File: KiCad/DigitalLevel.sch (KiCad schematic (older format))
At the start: 67 parts, among them SW1 SW_Push_Open, SW2 SW_Push_Open, SW3 SW_Push_Open, U2 MPU-6050, U3 XC6206P332MR

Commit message: Fixed schematics
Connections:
- net DIODE-SW renamed LED-SW
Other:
- moved on the sheet: C3
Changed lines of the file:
@@
 	1250 7400 1250 7600
-Wire Wire Line
-	1250 7600 1150 7600
 Wire Wire Line
 	3050 6850 3350 6850
@@
 	3350 7400 3350 7600
 Wire Wire Line
-	3350 7600 2350 7600
-Connection ~ 1250 7600
-Wire Wire Line
 	1650 6750 1550 6750
 Wire Wire Line
@@
 Wire Wire Line
 	1550 7400 1550 7600
-Connection ~ 1550 7600
-Wire Wire Line
-	1550 7600 1250 7600
 $Comp
 L Device:C C1
@@
 Wire Wire Line
 	3800 6750 3800 7100
-Connection ~ 3350 7600
 Wire Wire Line
 	2450 5850 2450 5750
@@
 	3800 7400 3800 7600
 Wire Wire Line
-	3350 7600 3800 7600
-Wire Wire Line
 	2250 5850 2250 5750
 Wire Wire Line
-	1150 6850 1150 7600
-Wire Wire Line
-	1150 6850 1650 6850
-Connection ~ 1150 7600
-Wire Wire Line
-	1150 7600 950  7600
-Wire Wire Line
-	1150 6850 800  6850
-Wire Wire Line
-	800  6850 800  6950
-Connection ~ 1150 6850
+	800  6850 800  7600
 $Comp
 L Device:C C3
 U 1 1 5E31CE3D
-P 800 7100
-F 0 "C3" H 915 7146 50  0000 L CNN
-F 1 "0.01u" H 915 7055 50  0000 L CNN
-F 2 "" H 838 6950 50  0001 C CNN
-F 3 "~" H 800 7100 50  0001 C CNN
-	1    800  7100
-	1    0    0    -1
-$EndComp
-Wire Wire Line
-	800  7250 800  7300
-Text GLabel 800  7300 3    50   Input ~ 0
+P 800 6700
+F 0 "C3" H 915 6746 50  0000 L CNN
+F 1 "0.01u" H 915 6655 50  0000 L CNN
+F 2 "" H 838 6550 50  0001 C CNN
+F 3 "~" H 800 6700 50  0001 C CNN
+	1    800  6700
+	-1   0    0    1
+$EndComp
+Wire Wire Line
+	800  6550 800  6500
+Text GLabel 800  6500 1    50   Input ~ 0
 VCC
 Wire Wire Line
@@
 $EndComp
 Wire Wire Line
-	1800 5350 1800 5300
-Wire Wire Line
 	2250 5750 2450 5750
 Connection ~ 2450 5750
@@
 Wire Wire Line
 	2350 7250 2350 7600
-Connection ~ 2350 7600
-Wire Wire Line
-	2350 7600 1550 7600
 Text GLabel 7550 2700 0    50   Input ~ 0
 VIN
@@
 	1050 1050 1050 1000
 Text GLabel 1050 1000 1    50   Input ~ 0
-DIODE-SW
+LED-SW
 Wire Wire Line
 	10300 1700 10300 1850
@@
 L power:GND #PWR?
 U 1 1 5E6CB783
-P 950 7600
-F 0 "#PWR?" H 950 7350 50  0001 C CNN
-F 1 "GND" H 955 7427 50  0000 C CNN
-F 2 "" H 950 7600 50  0001 C CNN
-F 3 "" H 950 7600 50  0001 C CNN
-	1    950  7600
-	1    0    0    -1
-$EndComp
-Wire Wire Line
-	1800 5300 1300 5300
-Wire Wire Line
-	1800 5750 2050 5750
-Wire Wire Line
-	1800 5750 1300 5750
-Wire Wire Line
-	1300 5750 1300 5850
-Connection ~ 1800 5750
-Wire Wire Line
-	1300 5300 1300 5200
+P 800 7600
+F 0 "#PWR?" H 800 7350 50  0001 C CNN
+F 1 "GND" H 805 7427 50  0000 C CNN
+F 2 "" H 800 7600 50  0001 C CNN
+F 3 "" H 800 7600 50  0001 C CNN
+	1    800  7600
+	1    0    0    -1
+$EndComp
 $Comp
 L power:GND #PWR?
 U 1 1 5E70F339
-P 1300 5850
-F 0 "#PWR?" H 1300 5600 50  0001 C CNN
-F 1 "GND" H 1305 5677 50  0000 C CNN
-F 2 "" H 1300 5850 50  0001 C CNN
-F 3 "" H 1300 5850 50  0001 C CNN
-	1    1300 5850
+P 1800 5750
+F 0 "#PWR?" H 1800 5500 50  0001 C CNN
+F 1 "GND" H 1805 5577 50  0000 C CNN
+F 2 "" H 1800 5750 50  0001 C CNN
+F 3 "" H 1800 5750 50  0001 C CNN
+	1    1800 5750
 	1    0    0    -1
 $EndComp
@@
 	9700 5400 9700 5550
 Connection ~ 9700 5550
-Text GLabel 1300 5200 1    50   Input ~ 0
+Text GLabel 1800 5350 1    50   Input ~ 0
 VCC
 Wire Wire Line
@@
 	1050 1850 2250 1850
 Connection ~ 2250 1850
+Connection ~ 800  6850
+Wire Wire Line
+	800  6850 1650 6850
+$Comp
+L power:GND #PWR?
+U 1 1 5E9579DB
+P 1250 7600
+F 0 "#PWR?" H 1250 7350 50  0001 C CNN
+F 1 "GND" H 1255 7427 50  0000 C CNN
+F 2 "" H 1250 7600 50  0001 C CNN
+F 3 "" H 1250 7600 50  0001 C CNN
+	1    1250 7600
+	1    0    0    -1
+$EndComp
+$Comp
+L power:GND #PWR?
+U 1 1 5E95E47C
+P 1550 7600
+F 0 "#PWR?" H 1550 7350 50  0001 C CNN
+F 1 "GND" H 1555 7427 50  0000 C CNN
+F 2 "" H 1550 7600 50  0001 C CNN
+F 3 "" H 1550 7600 50  0001 C CNN
+	1    1550 7600
+	1    0    0    -1
+$EndComp
+$Comp
+L power:GND #PWR?
+U 1 1 5E964EA6
+P 2350 7600
+F 0 "#PWR?" H 2350 7350 50  0001 C CNN
+F 1 "GND" H 2355 7427 50  0000 C CNN
+F 2 "" H 2350 7600 50  0001 C CNN
+F 3 "" H 2350 7600 50  0001 C CNN
+	1    2350 7600
+	1    0    0    -1
+$EndComp
+$Comp
+L power:GND #PWR?
+U 1 1 5E96B8D8
+P 3350 7600
+F 0 "#PWR?" H 3350 7350 50  0001 C CNN
+F 1 "GND" H 3355 7427 50  0000 C CNN
+F 2 "" H 3350 7600 50  0001 C CNN
+F 3 "" H 3350 7600 50  0001 C CNN
+	1    3350 7600
+	1    0    0    -1
+$EndComp
+$Comp
+L power:GND #PWR?
+U 1 1 5E972312
+P 3800 7600
+F 0 "#PWR?" H 3800 7350 50  0001 C CNN
+F 1 "GND" H 3805 7427 50  0000 C CNN
+F 2 "" H 3800 7600 50  0001 C CNN
+F 3 "" H 3800 7600 50  0001 C CNN
+	1    3800 7600
+	1    0    0    -1
+$EndComp
 $EndSCHEMATC

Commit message: Fixed schematics
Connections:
- net VCC: now also U?.24 (VDD)
- net VOUT: now also U?.9 (VDDA)
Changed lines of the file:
@@
 	1    0    0    -1
 $EndComp
+Wire Wire Line
+	3850 2450 3850 2250
+Text GLabel 3850 2250 1    50   Output ~ 0
+VCC
+Wire Wire Line
+	4150 2450 4150 2250
+Text GLabel 4150 2250 1    50   Input ~ 0
+VOUT
 $EndSCHEMATC

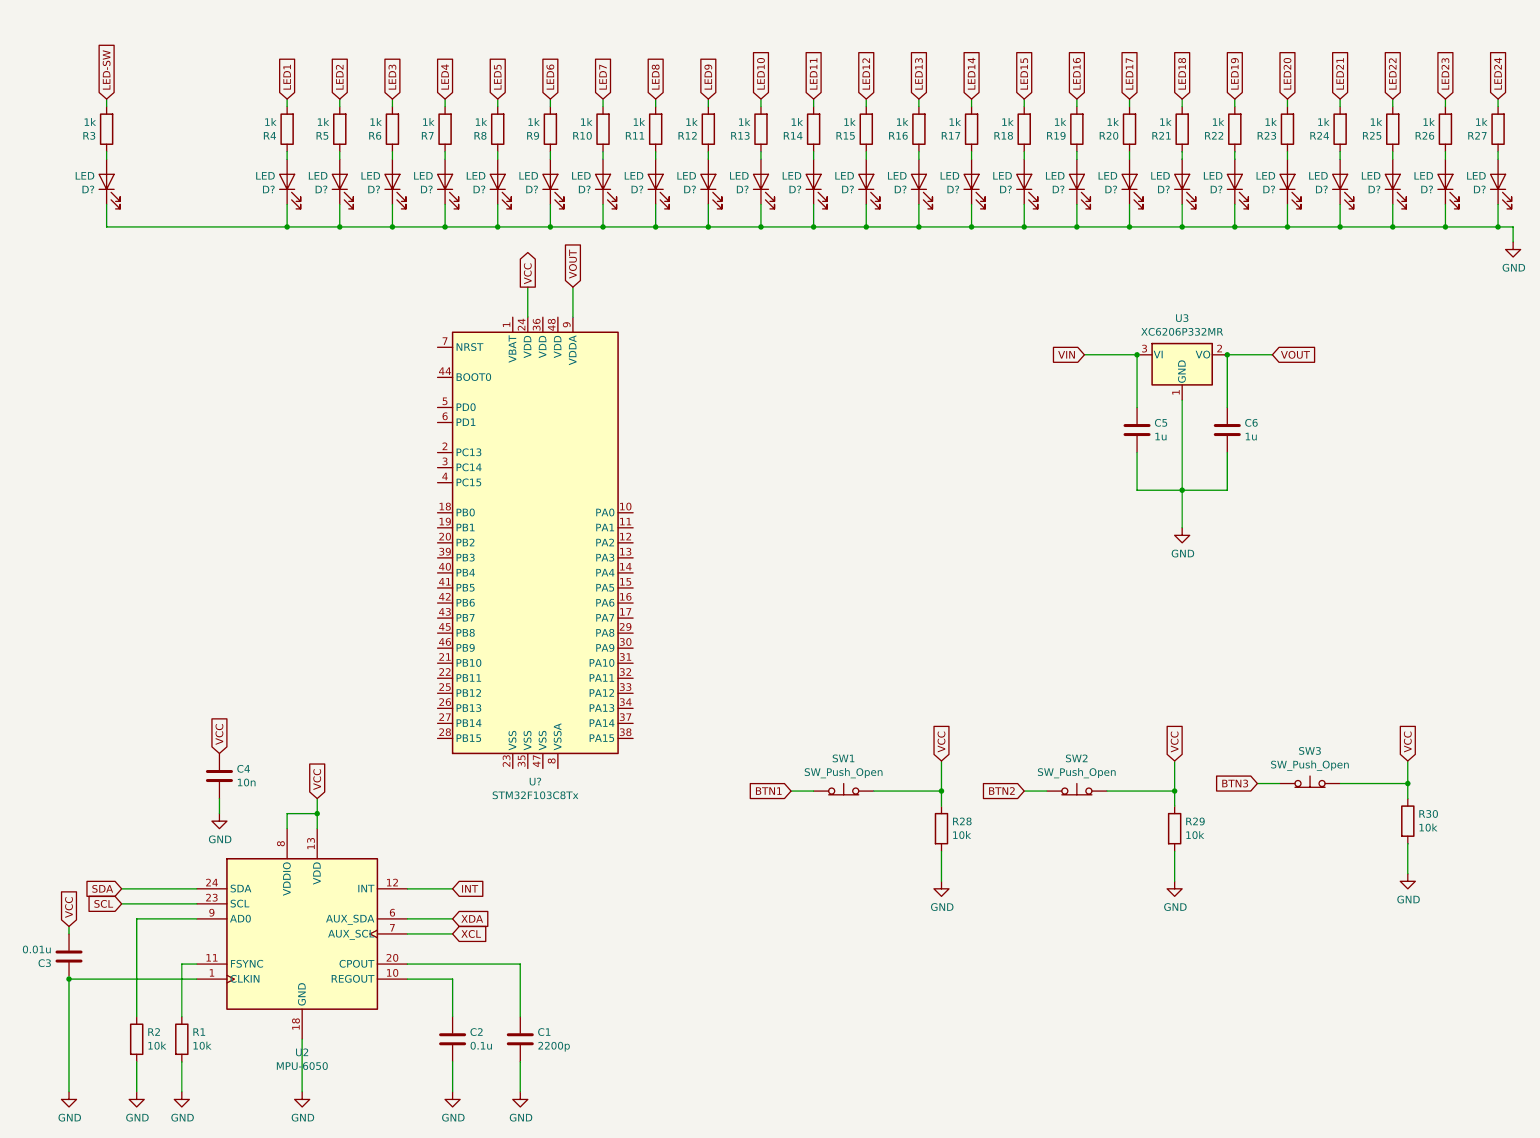
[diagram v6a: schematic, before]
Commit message: Fixed schematics
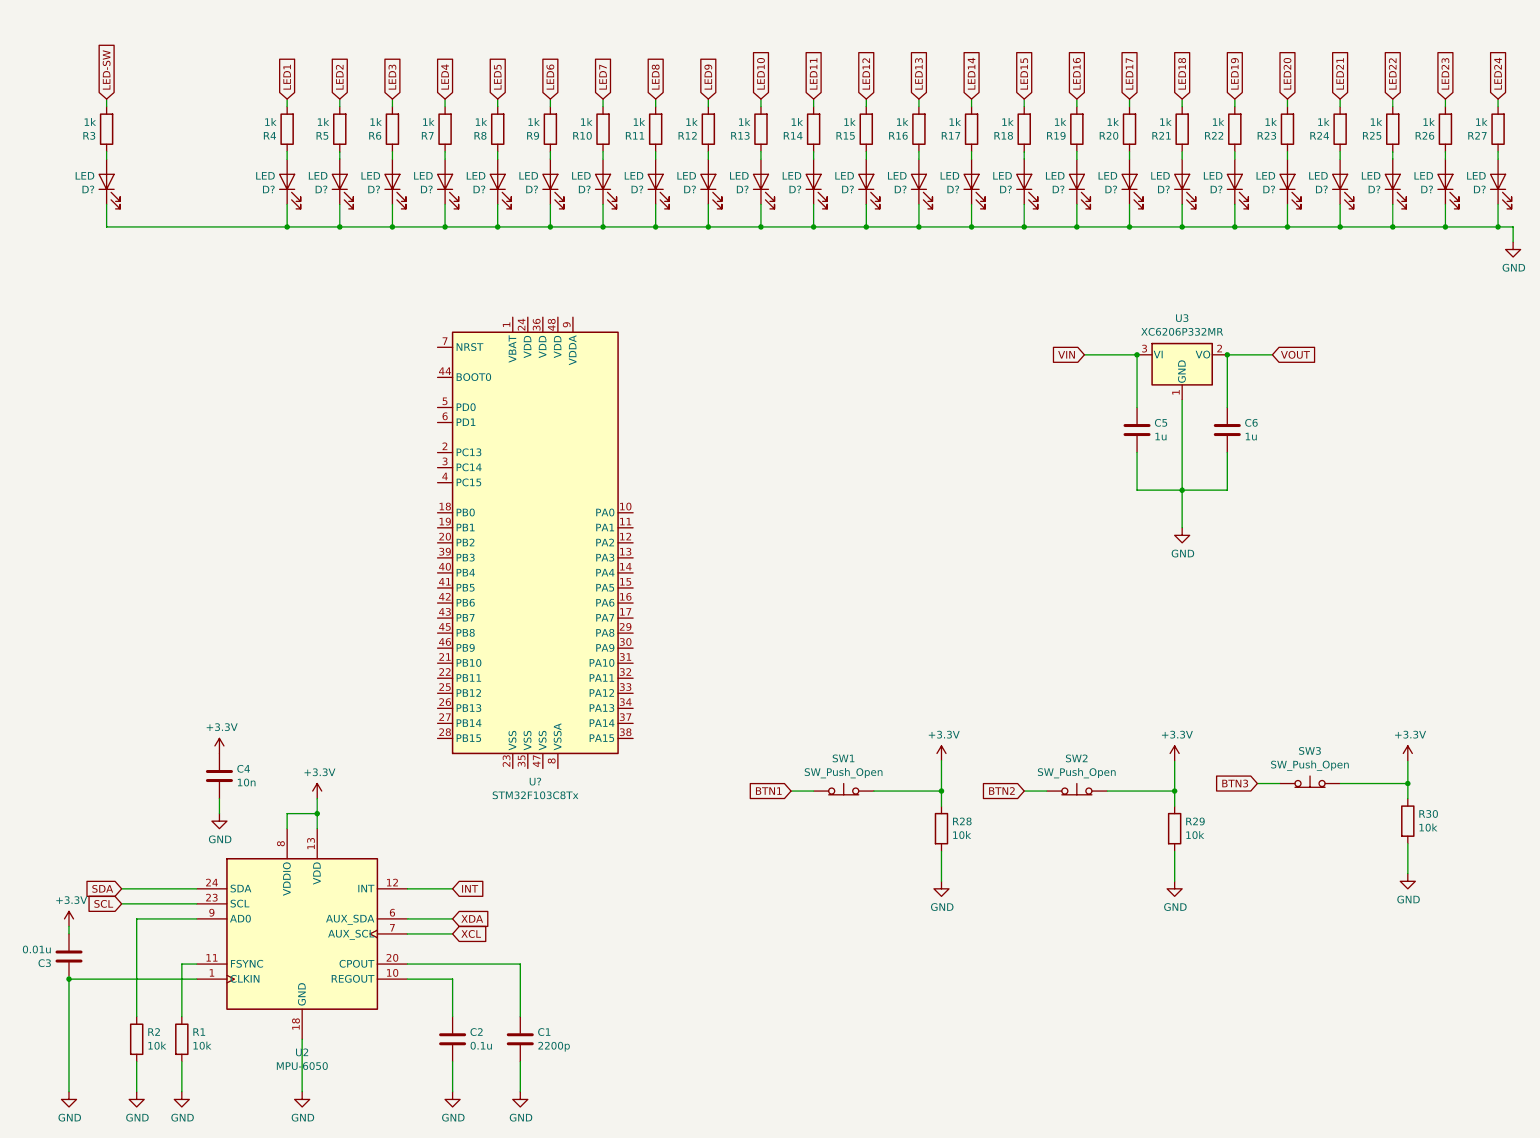
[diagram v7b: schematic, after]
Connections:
- net VOUT: no longer U?.9 (VDDA)
- net VCC renamed +3V3
- net +3V3: no longer U?.24 (VDD)
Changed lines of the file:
@@
 Wire Wire Line
 	2450 5850 2450 5750
-Text GLabel 2450 5650 1    50   Input ~ 0
-VCC
 Text GLabel 1150 6250 0    50   Input ~ 0
 SDA
@@
 Wire Wire Line
 	800  6550 800  6500
-Text GLabel 800  6500 1    50   Input ~ 0
-VCC
 Wire Wire Line
 	1800 5750 1800 5650
@@
 	1    0    0    -1
 $EndComp
-Text GLabel 6600 5400 1    50   Input ~ 0
-VCC
-Text GLabel 8150 5400 1    50   Input ~ 0
-VCC
-Text GLabel 9700 5400 1    50   Input ~ 0
-VCC
 Wire Wire Line
 	9700 5400 9700 5550
 Connection ~ 9700 5550
-Text GLabel 1800 5350 1    50   Input ~ 0
-VCC
 Wire Wire Line
 	8500 2700 8800 2700
@@
 	1    0    0    -1
 $EndComp
-Wire Wire Line
-	3850 2450 3850 2250
-Text GLabel 3850 2250 1    50   Output ~ 0
-VCC
-Wire Wire Line
-	4150 2450 4150 2250
-Text GLabel 4150 2250 1    50   Input ~ 0
-VOUT
+$Comp
+L power:+3.3V #PWR?
+U 1 1 5E99ED0A
+P 1800 5350
+F 0 "#PWR?" H 1800 5200 50  0001 C CNN
+F 1 "+3.3V" H 1815 5523 50  0000 C CNN
+F 2 "" H 1800 5350 50  0001 C CNN
+F 3 "" H 1800 5350 50  0001 C CNN
+	1    1800 5350
+	1    0    0    -1
+$EndComp
+$Comp
+L power:+3.3V #PWR?
+U 1 1 5E9A73F6
+P 800 6500
+F 0 "#PWR?" H 800 6350 50  0001 C CNN
+F 1 "+3.3V" H 815 6673 50  0000 C CNN
+F 2 "" H 800 6500 50  0001 C CNN
+F 3 "" H 800 6500 50  0001 C CNN
+	1    800  6500
+	1    0    0    -1
+$EndComp
+$Comp
+L power:+3.3V #PWR?
+U 1 1 5E9ADF66
+P 2450 5650
+F 0 "#PWR?" H 2450 5500 50  0001 C CNN
+F 1 "+3.3V" H 2465 5823 50  0000 C CNN
+F 2 "" H 2450 5650 50  0001 C CNN
+F 3 "" H 2450 5650 50  0001 C CNN
+	1    2450 5650
+	1    0    0    -1
+$EndComp
+$Comp
+L power:+3.3V #PWR?
+U 1 1 5E9B4D86
+P 6600 5400
+F 0 "#PWR?" H 6600 5250 50  0001 C CNN
+F 1 "+3.3V" H 6615 5573 50  0000 C CNN
+F 2 "" H 6600 5400 50  0001 C CNN
+F 3 "" H 6600 5400 50  0001 C CNN
+	1    6600 5400
+	1    0    0    -1
+$EndComp
+$Comp
+L power:+3.3V #PWR?
+U 1 1 5E9BB956
+P 8150 5400
+F 0 "#PWR?" H 8150 5250 50  0001 C CNN
+F 1 "+3.3V" H 8165 5573 50  0000 C CNN
+F 2 "" H 8150 5400 50  0001 C CNN
+F 3 "" H 8150 5400 50  0001 C CNN
+	1    8150 5400
+	1    0    0    -1
+$EndComp
+$Comp
+L power:+3.3V #PWR?
+U 1 1 5E9C25E4
+P 9700 5400
+F 0 "#PWR?" H 9700 5250 50  0001 C CNN
+F 1 "+3.3V" H 9715 5573 50  0000 C CNN
+F 2 "" H 9700 5400 50  0001 C CNN
+F 3 "" H 9700 5400 50  0001 C CNN
+	1    9700 5400
+	1    0    0    -1
+$EndComp
 $EndSCHEMATC
